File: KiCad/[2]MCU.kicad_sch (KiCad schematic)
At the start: 13 parts, among them J200 Conn_01x04_Pin, J201 Conn_01x04_Pin, SW200 SW_DPDT_XLX, U200 RaspberryPi_Pico, U202 mems-mic, U203 mems-mic

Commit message: Manufacture files preparation
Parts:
- J200, J201, SW200, U200, U202, U203: now not fitted
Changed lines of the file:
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@@
 		(in_bom yes)
 		(on_board yes)
-		(dnp no)
+		(dnp yes)
 		(property "Reference" "U203"
 			(at 78.74 172.7514 0)
@@
 		(in_bom yes)
 		(on_board yes)
-		(dnp no)
+		(dnp yes)
 		(fields_autoplaced yes)
 		(property "Reference" "U202"
@@
 		(on_board yes)
 		(dnp no)
-		(property "Reference" "#PWR66"
+		(property "Reference" "#PWR066"
 			(at 269.24 123.19 0)
 			(effects
@@
 			(project "rpi_pico_media_board"
 				(path "/883c739e-d2a5-4bc8-a050-29a6043b4072/c11951ca-d234-4f4a-995a-10451a30b94e"
-					(reference "#PWR66")
+					(reference "#PWR066")
 					(unit 1)
 				)
@@
 		(on_board yes)
 		(dnp no)
-		(property "Reference" "#PWR63"
+		(property "Reference" "#PWR063"
 			(at 220.98 62.23 0)
 			(effects
@@
 			(project "rpi_pico_media_board"
 				(path "/883c739e-d2a5-4bc8-a050-29a6043b4072/c11951ca-d234-4f4a-995a-10451a30b94e"
-					(reference "#PWR63")
+					(reference "#PWR063")
 					(unit 1)
 				)
@@
 		(in_bom yes)
 		(on_board yes)
-		(dnp no)
+		(dnp yes)
 		(fields_autoplaced yes)
 		(property "Reference" "SW200"
@@
 		(in_bom yes)
 		(on_board yes)
-		(dnp no)
+		(dnp yes)
 		(property "Reference" "J200"
 			(at 257.175 46.99 0)
@@
 		(on_board yes)
 		(dnp no)
-		(property "Reference" "#PWR50"
+		(property "Reference" "#PWR050"
 			(at 63.5 166.37 0)
 			(effects
@@
 			(project "rpi_pico_media_board"
 				(path "/883c739e-d2a5-4bc8-a050-29a6043b4072/c11951ca-d234-4f4a-995a-10451a30b94e"
-					(reference "#PWR50")
+					(reference "#PWR050")
 					(unit 1)
 				)
@@
 		(on_board yes)
 		(dnp no)
-		(property "Reference" "#PWR65"
+		(property "Reference" "#PWR065"
 			(at 242.57 87.63 0)
 			(effects
@@
 			(project "rpi_pico_media_board"
 				(path "/883c739e-d2a5-4bc8-a050-29a6043b4072/c11951ca-d234-4f4a-995a-10451a30b94e"
-					(reference "#PWR65")
+					(reference "#PWR065")
 					(unit 1)
 				)
@@
 			)
 		)
-		(property "Manufacturer_Name" ""
-			(at 201.93 31.75 0)
-			(effects
-				(font
-					(size 1.27 1.27)
-				)
-				(hide yes)
-			)
-		)
-		(property "Manufacturer_Part_Number" ""
-			(at 201.93 31.75 0)
-			(effects
-				(font
-					(size 1.27 1.27)
-				)
-				(hide yes)
-			)
-		)
 		(property "Manufacturer" "Nexperia"
 			(at 201.93 31.75 0)
@@
 		(on_board yes)
 		(dnp no)
-		(property "Reference" "#PWR52"
+		(property "Reference" "#PWR052"
 			(at 63.5 143.51 0)
 			(effects
@@
 			(project "rpi_pico_media_board"
 				(path "/883c739e-d2a5-4bc8-a050-29a6043b4072/c11951ca-d234-4f4a-995a-10451a30b94e"
-					(reference "#PWR52")
+					(reference "#PWR052")
 					(unit 1)
 				)
@@
 		(in_bom yes)
 		(on_board yes)
-		(dnp no)
+		(dnp yes)
 		(fields_autoplaced yes)
 		(property "Reference" "U200"
@@
 		(on_board yes)
 		(dnp no)
-		(property "Reference" "#PWR55"
+		(property "Reference" "#PWR055"
 			(at 63.5 195.58 0)
 			(effects
@@
 			(project "rpi_pico_media_board"
 				(path "/883c739e-d2a5-4bc8-a050-29a6043b4072/c11951ca-d234-4f4a-995a-10451a30b94e"
-					(reference "#PWR55")
+					(reference "#PWR055")
 					(unit 1)
 				)
@@
 		(on_board yes)
 		(dnp no)
-		(property "Reference" "#PWR68"
+		(property "Reference" "#PWR068"
 			(at 220.98 113.03 0)
 			(effects
@@
 			(project "rpi_pico_media_board"
 				(path "/883c739e-d2a5-4bc8-a050-29a6043b4072/c11951ca-d234-4f4a-995a-10451a30b94e"
-					(reference "#PWR68")
+					(reference "#PWR068")
 					(unit 1)
 				)
@@
 		(on_board yes)
 		(dnp no)
-		(property "Reference" "#PWR67"
+		(property "Reference" "#PWR067"
 			(at 242.57 143.51 0)
 			(effects
@@
 			(project "rpi_pico_media_board"
 				(path "/883c739e-d2a5-4bc8-a050-29a6043b4072/c11951ca-d234-4f4a-995a-10451a30b94e"
-					(reference "#PWR67")
+					(reference "#PWR067")
 					(unit 1)
 				)
@@
 		(in_bom yes)
 		(on_board yes)
-		(dnp no)
+		(dnp yes)
 		(property "Reference" "J201"
 			(at 257.175 102.87 0)
@@
 		(dnp no)
 		(fields_autoplaced yes)
-		(property "Reference" "#PWR49"
+		(property "Reference" "#PWR049"
 			(at 208.28 34.29 0)
 			(effects
@@
 			(project "rpi_pico_media_board"
 				(path "/883c739e-d2a5-4bc8-a050-29a6043b4072/c11951ca-d234-4f4a-995a-10451a30b94e"
-					(reference "#PWR49")
+					(reference "#PWR049")
 					(unit 1)
 				)
@@
 		(on_board yes)
 		(dnp no)
-		(property "Reference" "#PWR54"
+		(property "Reference" "#PWR054"
 			(at 63.5 173.99 0)
 			(effects
@@
 			(project "rpi_pico_media_board"
 				(path "/883c739e-d2a5-4bc8-a050-29a6043b4072/c11951ca-d234-4f4a-995a-10451a30b94e"
-					(reference "#PWR54")
+					(reference "#PWR054")
 					(unit 1)
 				)
@@
 		(dnp no)
 		(fields_autoplaced yes)
-		(property "Reference" "#PWR33"
+		(property "Reference" "#PWR033"
 			(at 162.56 50.8 0)
 			(effects
@@
 			(project ""
 				(path "/883c739e-d2a5-4bc8-a050-29a6043b4072/c11951ca-d234-4f4a-995a-10451a30b94e"
-					(reference "#PWR33")
+					(reference "#PWR033")
 					(unit 1)
 				)
@@
 		(on_board yes)
 		(dnp no)
-		(property "Reference" "#PWR32"
+		(property "Reference" "#PWR032"
 			(at 153.67 144.78 0)
 			(effects
@@
 			(project "rpi_pico_media_board"
 				(path "/883c739e-d2a5-4bc8-a050-29a6043b4072/c11951ca-d234-4f4a-995a-10451a30b94e"
-					(reference "#PWR32")
+					(reference "#PWR032")
 					(unit 1)
 				)
@@
 		(on_board yes)
 		(dnp no)
-		(property "Reference" "#PWR64"
+		(property "Reference" "#PWR064"
 			(at 271.78 63.5 0)
 			(effects
@@
 			(project "rpi_pico_media_board"
 				(path "/883c739e-d2a5-4bc8-a050-29a6043b4072/c11951ca-d234-4f4a-995a-10451a30b94e"
-					(reference "#PWR64")
-					(unit 1)
-				)
+					(reference "#PWR064")
+					(unit 1)
+				)

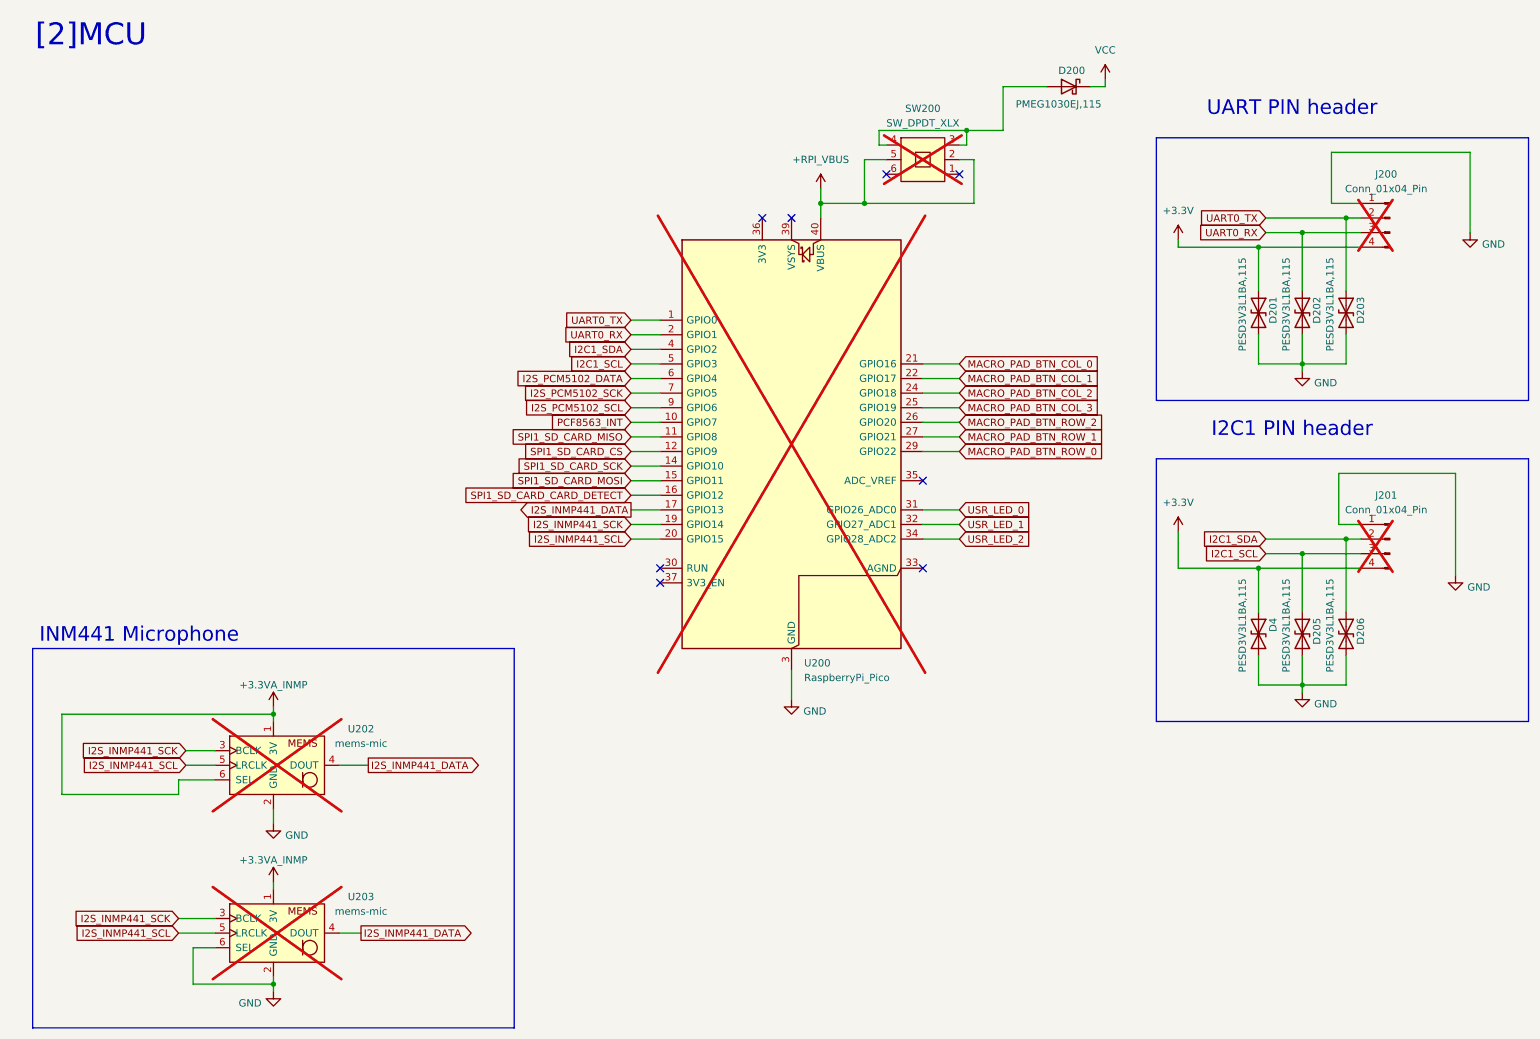
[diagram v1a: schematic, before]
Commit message: First fixes after board assembly
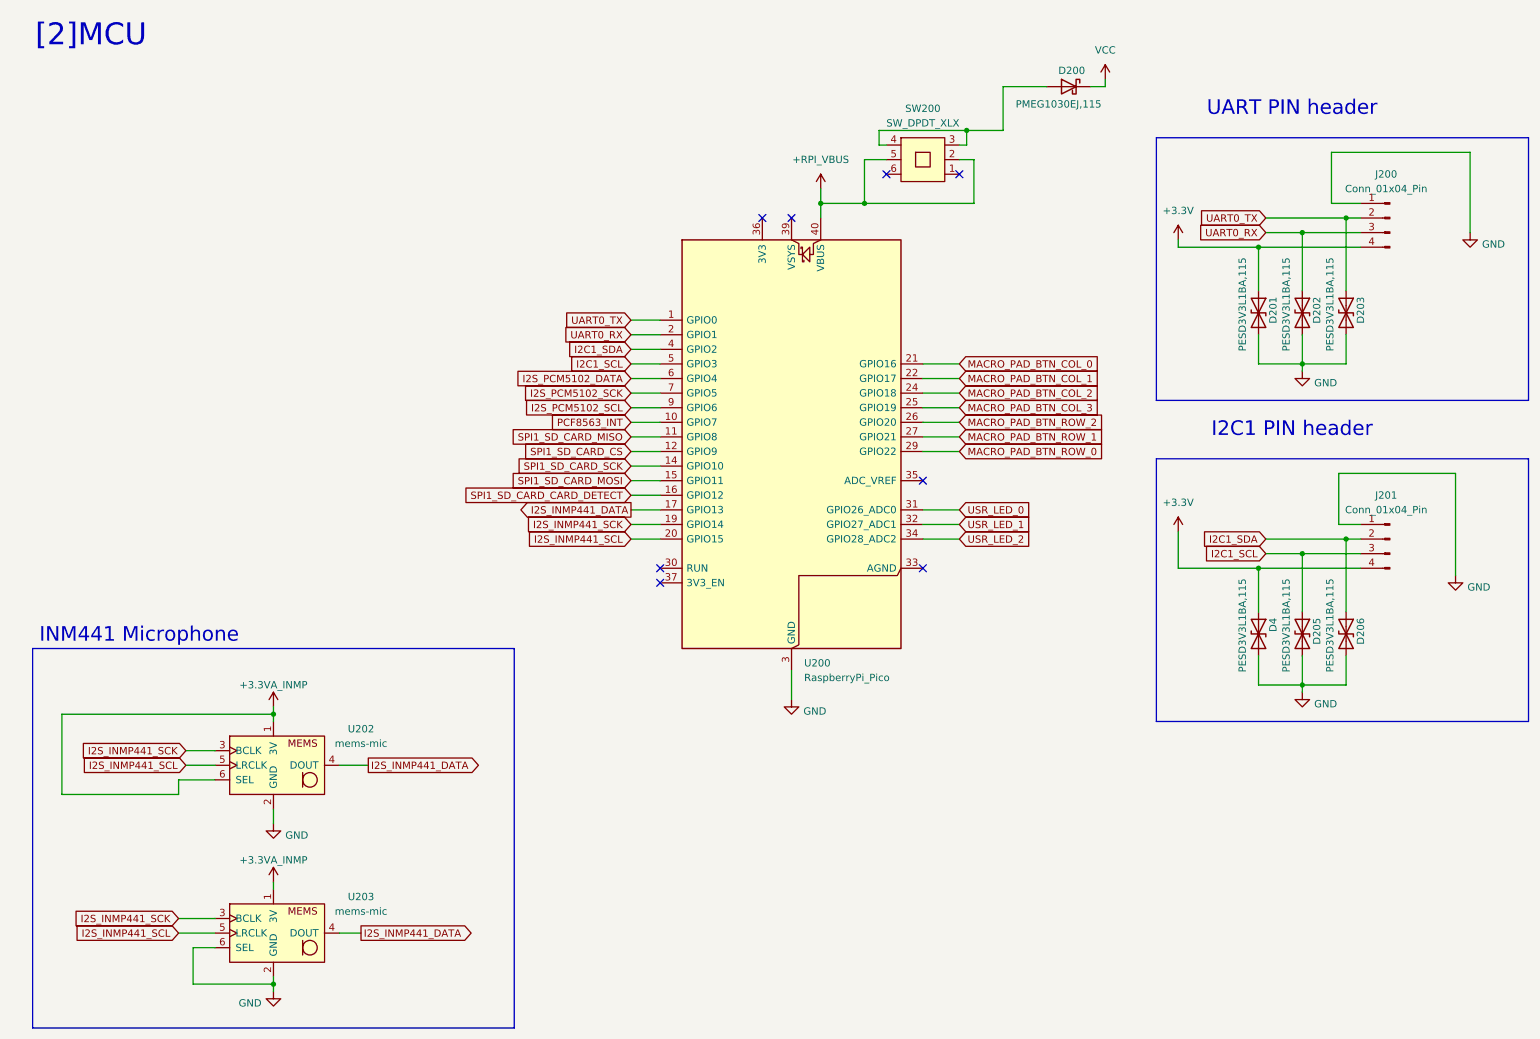
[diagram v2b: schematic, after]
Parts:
- J200, J201, SW200, U200, U202, U203: now fitted
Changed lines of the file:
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@@
 (kicad_sch
-	(version 20231120)
+	(version 20250114)
 	(generator "eeschema")
-	(generator_version "8.0")
+	(generator_version "9.0")
 	(paper "A4")
+	(rectangle
+		(start 217.17 96.52)
+		(end 281.94 142.24)
+		(stroke
+			(width 0)
+			(type default)
+		)
+		(fill
+			(type none)
+		)
+	)
+	(rectangle
+		(start 217.17 40.64)
+		(end 281.94 86.36)
+		(stroke
+			(width 0)
+			(type default)
+		)
+		(fill
+			(type none)
+		)
+	)
+	(rectangle
+		(start 21.59 129.54)
+		(end 105.41 195.58)
+		(stroke
+			(width 0)
+			(type default)
+		)
+		(fill
+			(type none)
+		)
+	)
+	(text "INM441 Microphone"
+		(exclude_from_sim no)
+		(at 40.132 127.254 0)
+		(effects
+			(font
+				(size 2.54 2.54)
+			)
+		)
+	)
+	(text "UART PIN header"
+		(exclude_from_sim no)
+		(at 240.792 35.56 0)
+		(effects
+			(font
+				(size 2.54 2.54)
+			)
+		)
+	)
+	(text "I2C1 PIN header"
+		(exclude_from_sim no)
+		(at 240.792 91.44 0)
+		(effects
+			(font
+				(size 2.54 2.54)
+			)
+		)
+	)
+	(text "[2]MCU"
+		(exclude_from_sim no)
+		(at 31.75 22.86 0)
+		(effects
+			(font
+				(size 3.81 3.81)
+			)
+		)
+	)
 	(junction
 		(at 63.5 140.97)
@@
 		)
 	)
-	(rectangle
-		(start 217.17 96.52)
-		(end 281.94 142.24)
-		(stroke
-			(width 0)
-			(type default)
-		)
-		(fill
-			(type none)
-		)
-	)
-	(rectangle
-		(start 217.17 40.64)
-		(end 281.94 86.36)
-		(stroke
-			(width 0)
-			(type default)
-		)
-		(fill
-			(type none)
-		)
-	)
-	(rectangle
-		(start 21.59 129.54)
-		(end 105.41 195.58)
-		(stroke
-			(width 0)
-			(type default)
-		)
-		(fill
-			(type none)
-		)
-	)
-	(text "INM441 Microphone"
-		(exclude_from_sim no)
-		(at 40.132 127.254 0)
-		(effects
-			(font
-				(size 2.54 2.54)
-			)
-		)
-	)
-	(text "UART PIN header"
-		(exclude_from_sim no)
-		(at 240.792 35.56 0)
-		(effects
-			(font
-				(size 2.54 2.54)
-			)
-		)
-	)
-	(text "I2C1 PIN header"
-		(exclude_from_sim no)
-		(at 240.792 91.44 0)
-		(effects
-			(font
-				(size 2.54 2.54)
-			)
-		)
-	)
-	(text "[2]MCU"
-		(exclude_from_sim no)
-		(at 31.75 22.86 0)
-		(effects
-			(font
-				(size 3.81 3.81)
-			)
-		)
-	)
 	(global_label "UART0_TX"
 		(shape input)
@@
 		(in_bom yes)
 		(on_board yes)
-		(dnp yes)
+		(dnp no)
 		(property "Reference" "U203"
 			(at 78.74 172.7514 0)
@@
 		(in_bom yes)
 		(on_board yes)
-		(dnp yes)
+		(dnp no)
 		(fields_autoplaced yes)
 		(property "Reference" "U202"
@@
 		(in_bom yes)
 		(on_board yes)
-		(dnp yes)
+		(dnp no)
 		(fields_autoplaced yes)
 		(property "Reference" "SW200"
@@
 		(in_bom yes)
 		(on_board yes)
-		(dnp yes)
+		(dnp no)
 		(property "Reference" "J200"
 			(at 257.175 46.99 0)
@@
 		(in_bom yes)
 		(on_board yes)
-		(dnp yes)
+		(dnp no)
 		(fields_autoplaced yes)
 		(property "Reference" "U200"
@@
 		(in_bom yes)
 		(on_board yes)
-		(dnp yes)
+		(dnp no)
 		(property "Reference" "J201"
 			(at 257.175 102.87 0)
